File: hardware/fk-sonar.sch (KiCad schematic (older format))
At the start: 73 parts, among them J1 Conn_01x03, J2 CONN_02x05_SWD, J3 RF-SMA-EDGE, J4 MICRO-USB, J5 S2B-PH-SM4-TB, J6 CONN_01x04, J7 S2B-PH-SM4-TB, J8 CONN_01x03_SERIAL, J9 Conn_01x05, M1 MOUNT_HOLE, M2 FIDUCIAL, M3 MOUNT_HOLE, M4 MOUNT_HOLE, M5 FIDUCIAL, M6 MOUNT_HOLE, Q1 2N7002LT1G, SW1 SPNO, U1 ATSAMD21G18A-AU, U2 RFM95W, U3 BQ24074RGTT, U4 S25FL116K0XMFI041, U5 MAX1704XX, U6 MCP1700T-3302E/MB, U7 SK6812, Y1 FC-135

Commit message: Fix SK6812. Assign easier to read labels to signals.
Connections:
- net labels added: D2_RADIO_CS, D38_RADIO_D0, D5, D6_FLASH_CS
- net labels removed: FLASH_CS, RADIO_CS, RADIO_D0, SD_CS, WIFI_CS, WIFI_EN, WIFI_IRQ, WIFI_RST, WIFI_WAKE

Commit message: Align connectors on side. Add periph switch.
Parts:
- added C22, C23: 100nF, conservify:CAP-0603, symbol fk-sonar-rescue:CAPACITOR-CERAMIC
- added C24: 10uF, conservify:CAP-0603, symbol fk-sonar-rescue:CAPACITOR-CERAMIC
- added J10: CONN_01x02, conservify:SJ_OPEN, symbol conservify:CONN_01x02
- added R4: 10K, conservify:RES-0603, symbol conservify:RESISTOR
- added U8: TPS2051B, conservify:SOT-23-5_HandSoldering, symbol conservify:TPS2051B
- J1: value Conn_01x03 -> CONN_01x03
- J9: value Conn_01x05 -> CONN_01x05
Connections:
- net labels added: D8_PERIPH_EN, PERIPH_3V3
- net labels removed: D8
- wire segments 339 -> 356
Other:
- note added: "CONNECTORS"
- note removed: "1. All capacitors are NP0/COG 50V unless specified.\n2. All resistors are 62.5mW 1% unless specified."
- note removed: "NOTES"
- moved on the sheet: J2, J8

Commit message: Fixing rescued stuff and DRC checks.
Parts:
- C1, C10, C11, C12, C13, C14, C15, C16, C17, C18, C19, C2, C20, C21, C22, C23, C24, C3, C4, C5, C6, C7, C8, C9: symbol fk-sonar-rescue:CAPACITOR-CERAMIC -> conservify:CAPACITOR_CERAMIC
- D1, D7, D8: symbol fk-sonar-rescue:LED-SINGLE -> conservify:LED_SINGLE
- D5: symbol fk-sonar-rescue:DIODE_DUAL_Schottky -> conservify:DIODE_DUAL_SCHOTTKY
- J1: symbol fk-sonar-rescue:Conn_01x03 -> conservify:CONN_01x03
- J3: symbol fk-sonar-rescue:RF-SMA-EDGE -> conservify:RF_SMA_EDGE
- J4: symbol fk-sonar-rescue:MICRO-USB -> conservify:MICRO_USB
- J5, J7: symbol fk-sonar-rescue:S2B-PH-SM4-TB -> conservify:S2B_PH_SM4_TB
- J6: symbol fk-sonar-rescue:Conn_01x04 -> conservify:CONN_01x04
- J9: symbol fk-sonar-rescue:Conn_01x05 -> conservify:CONN_01x05
- Q1: symbol fk-sonar-rescue:MOSFET-N -> conservify:MOSFET_N
- SW1: symbol fk-sonar-rescue:TACT-SWITCH_2Pins -> conservify:SWITCH_CONN_02
- U1: symbol fk-sonar-rescue:ATSAMD21G18A-AU -> conservify:ATSAMD21G18A_AU
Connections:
- net labels removed: AREF
- wire segments 356 -> 359
- no-connect marks 19 -> 33

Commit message: Use more compatible FP for flash.
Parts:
- U4: footprint conservify:SOIC-8-N -> conservify:SOIC-8-N-WIDE
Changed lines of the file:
@@
 F 0 "U4" H 13750 7200 60  0000 C CNN
 F 1 "S25FL116K0XMFI041" H 13750 6600 60  0000 C CNN
-F 2 "conservify:SOIC-8-N" H 13750 6500 60  0001 C CNN
+F 2 "conservify:SOIC-8-N-WIDE" H 13750 6500 60  0001 C CNN
 F 3 "" H 13550 6950 60  0000 C CNN
 F 4 " " H 13750 7300 50  0001 C CNN "Critical"

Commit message: Consistency in part values
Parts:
- C24: MFN Murata Electronics -> Taiyo Yuden; MFP (none) -> LMK107BBJ106KALT; SPN1 (none) -> 963-LMK107BBJ106KALT
- J10: Critical (none) -> (none); MFN (none) -> (none); MFP (none) -> (none); Notes (none) -> (none); Package (none) -> (none); SPN1 (none) -> (none); Source (none) -> ANY; Subsystem (none) -> (none); Supplier1 (none) -> (none)
- J6: MFN (none) -> Molex; MFP (none) -> 502382-0470; SPN1 (none) -> WM4781CT-ND; Supplier1 (none) -> digikey
- U8: Critical (none) -> (none); MFN (none) -> Texas Instruments; MFP (none) -> TPS2051BDBVR; Notes (none) -> (none); Package (none) -> (none); SPN1 (none) -> 296-21265-1-ND; Source (none) -> ANY; Subsystem (none) -> (none); Supplier1 (none) -> digikey

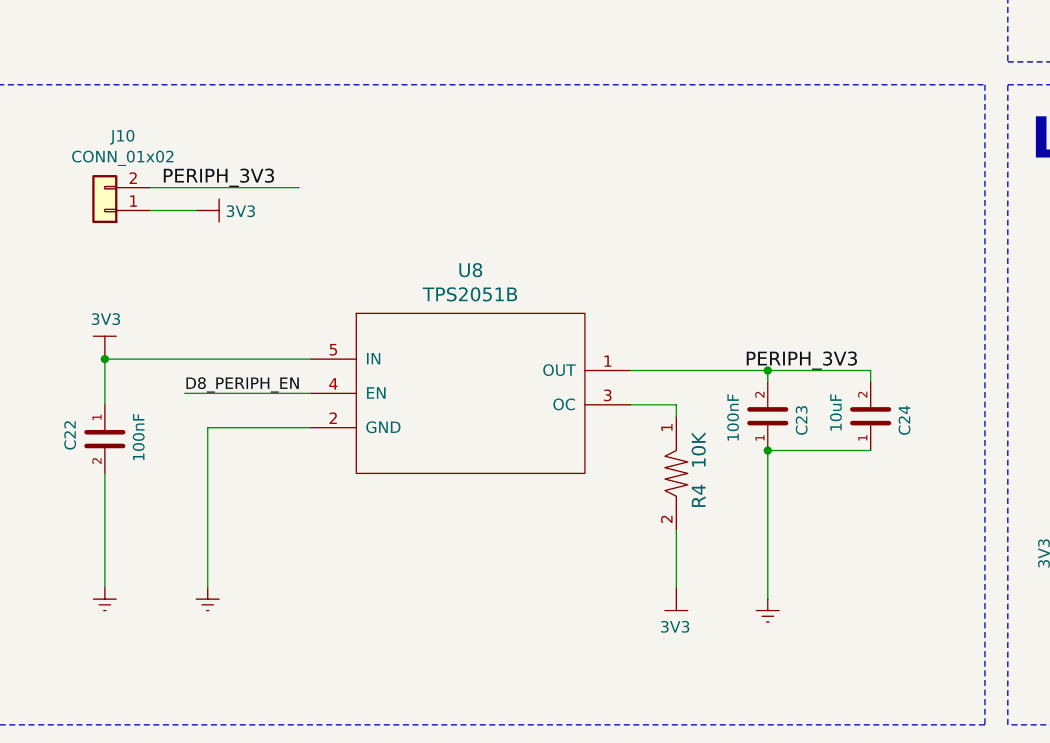
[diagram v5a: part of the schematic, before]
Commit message: Adding some pull downs.
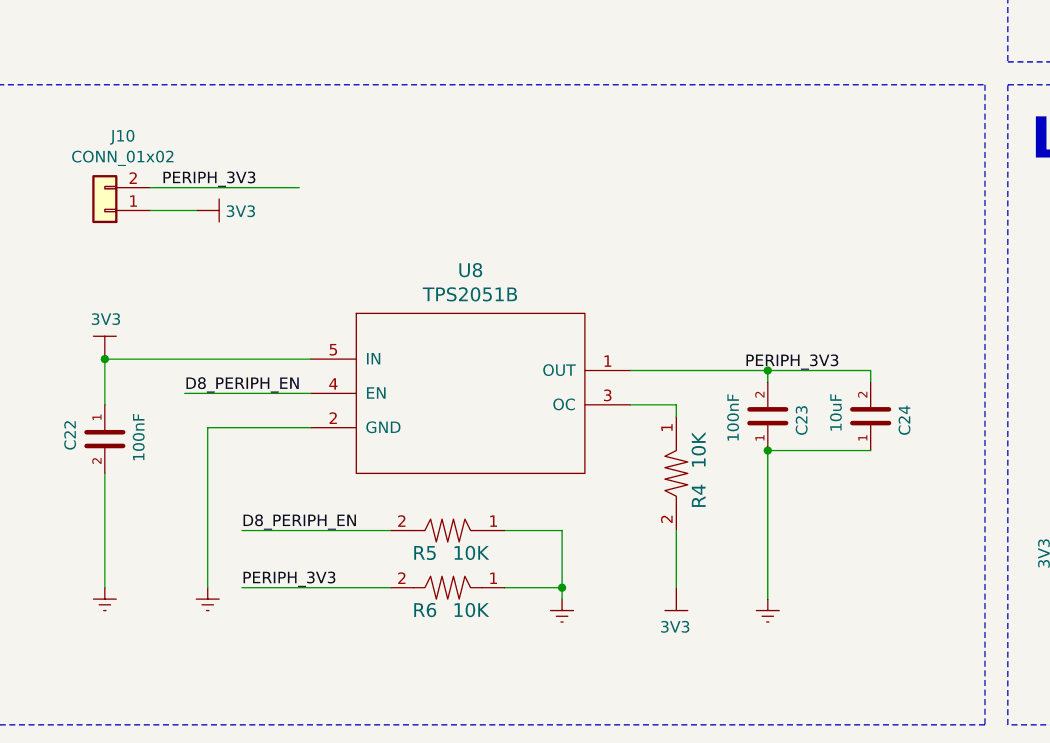
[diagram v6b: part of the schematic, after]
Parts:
- added R5, R6: 10K, conservify:RES-0603, symbol conservify:RESISTOR
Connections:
- wire segments 359 -> 365
